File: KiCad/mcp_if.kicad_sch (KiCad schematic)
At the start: 11 parts

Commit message: Made the board :D
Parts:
- D10, D12, D8: footprint Diode_THT:D_5W_P5.08mm_Vertical_KathodeUp -> LED_THT:LED_D5.0mm
- D11, D13, D9: footprint Diode_THT:D_5W_P5.08mm_Vertical_AnodeUp -> LED_THT:LED_D5.0mm
- R10, R11, R9: footprint Resistor_THT:R_Axial_DIN0204_L3.6mm_D1.6mm_P2.54mm_Vertical -> Resistor_THT:R_Axial_DIN0207_L6.3mm_D2.5mm_P7.62mm_Horizontal
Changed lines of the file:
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@@
 			)
 		)
-		(property "Footprint" "Diode_THT:D_5W_P5.08mm_Vertical_AnodeUp"
+		(property "Footprint" "LED_THT:LED_D5.0mm"
 			(at 48.26 62.23 0)
 			(effects
@@
 			)
 		)
-		(property "Footprint" "Resistor_THT:R_Axial_DIN0204_L3.6mm_D1.6mm_P2.54mm_Vertical"
+		(property "Footprint" "Resistor_THT:R_Axial_DIN0207_L6.3mm_D2.5mm_P7.62mm_Horizontal"
 			(at 139.7 58.42 0)
 			(effects
@@
 			)
 		)
-		(property "Footprint" "Diode_THT:D_5W_P5.08mm_Vertical_KathodeUp"
+		(property "Footprint" "LED_THT:LED_D5.0mm"
 			(at 148.59 33.02 0)
 			(effects
@@
 			)
 		)
-		(property "Footprint" "Diode_THT:D_5W_P5.08mm_Vertical_AnodeUp"
+		(property "Footprint" "LED_THT:LED_D5.0mm"
 			(at 148.59 40.64 0)
 			(effects
@@
 			)
 		)
-		(property "Footprint" "Diode_THT:D_5W_P5.08mm_Vertical_KathodeUp"
+		(property "Footprint" "LED_THT:LED_D5.0mm"
 			(at 148.59 54.61 0)
 			(effects
@@
 			)
 		)
-		(property "Footprint" "Diode_THT:D_5W_P5.08mm_Vertical_AnodeUp"
+		(property "Footprint" "LED_THT:LED_D5.0mm"
 			(at 148.59 62.23 0)
 			(effects
@@
 			)
 		)
-		(property "Footprint" "Diode_THT:D_5W_P5.08mm_Vertical_KathodeUp"
+		(property "Footprint" "LED_THT:LED_D5.0mm"
 			(at 48.26 54.61 0)
 			(effects
@@
 			)
 		)
-		(property "Footprint" "Resistor_THT:R_Axial_DIN0204_L3.6mm_D1.6mm_P2.54mm_Vertical"
+		(property "Footprint" "Resistor_THT:R_Axial_DIN0207_L6.3mm_D2.5mm_P7.62mm_Horizontal"
 			(at 39.37 58.42 0)
 			(effects
@@
 			)
 		)
-		(property "Footprint" "Resistor_THT:R_Axial_DIN0204_L3.6mm_D1.6mm_P2.54mm_Vertical"
+		(property "Footprint" "Resistor_THT:R_Axial_DIN0207_L6.3mm_D2.5mm_P7.62mm_Horizontal"
 			(at 139.7 36.83 0)
 			(effects

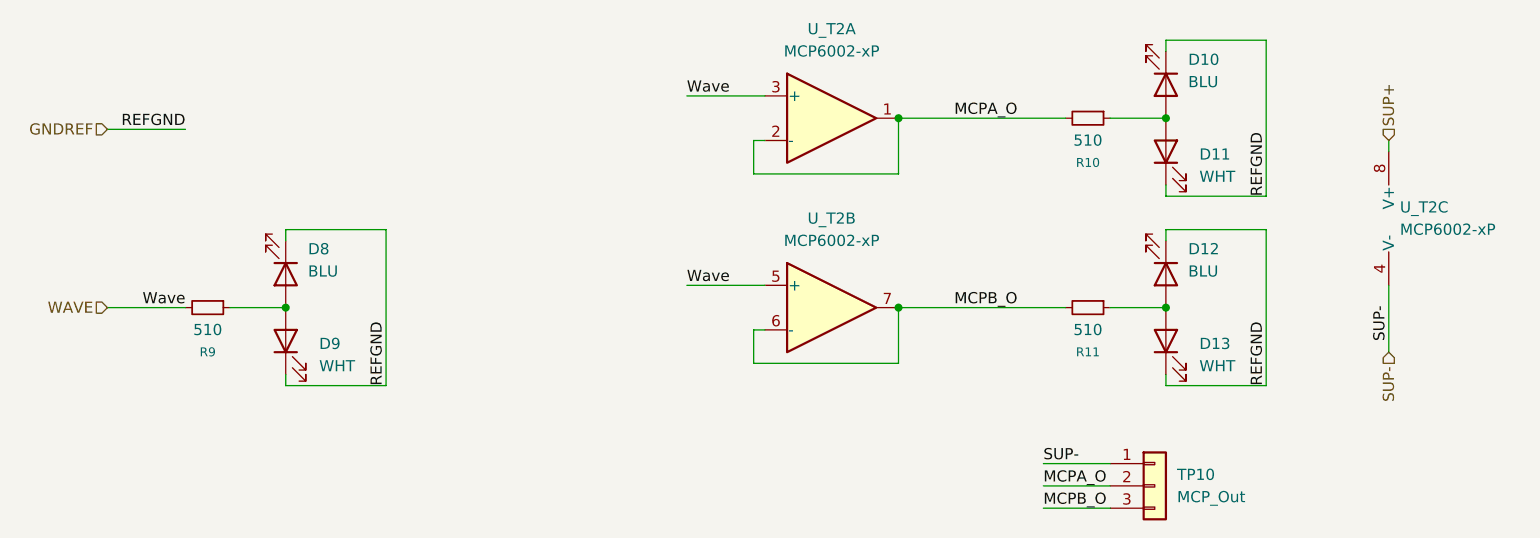
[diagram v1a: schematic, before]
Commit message: Added milling machine files / updated schematic+pcb annotations /  updated footprints
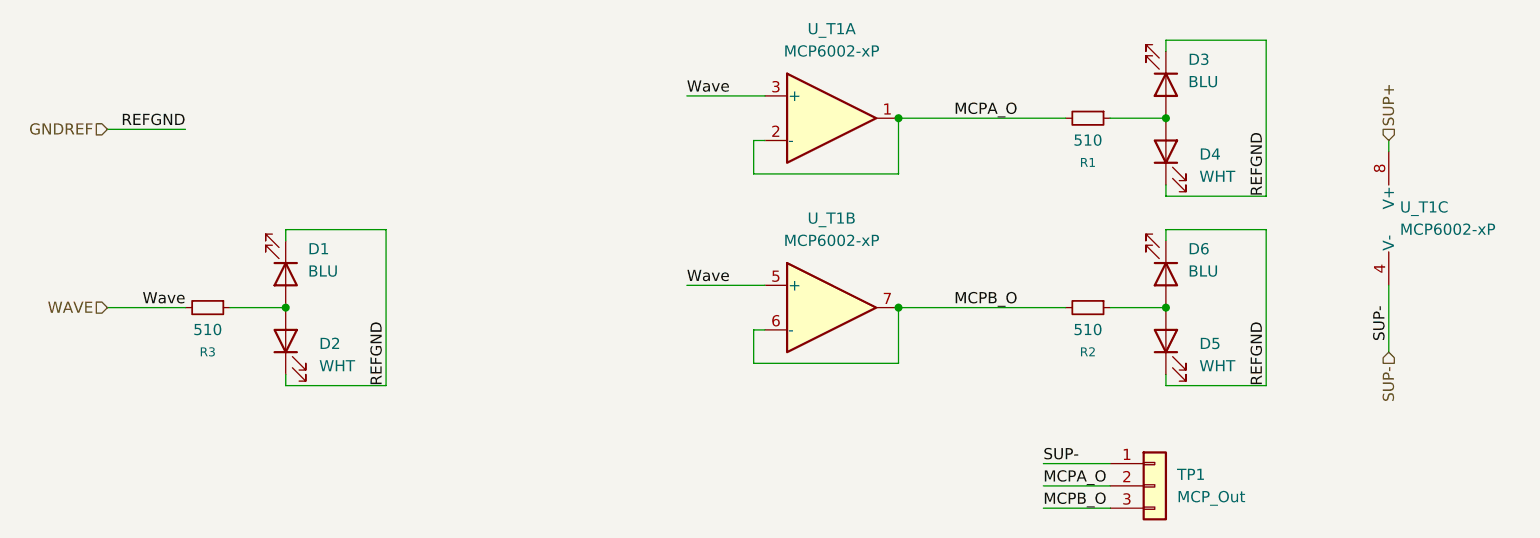
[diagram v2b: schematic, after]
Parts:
- renumbered D8 to D1, D9 to D2, D10 to D3, D11 to D4, D13 to D5, D12 to D6, R10 to R1, R11 to R2, R9 to R3, TP10 to TP1, U_T2 to U_T1
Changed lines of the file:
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@@
 		(dnp no)
 		(fields_autoplaced yes)
-		(property "Reference" "D9"
+		(property "Reference" "D2"
 			(at 52.07 62.5474 90)
 			(effects
@@
 			(project "ChipTester_354"
 				(path "/57b9e980-cd8f-44e4-af61-2cbd5bb30325/66abbfc5-c7ee-42ee-8f01-bf5211a4ea1c"
-					(reference "D9")
+					(reference "D2")
 					(unit 1)
 				)
@@
 		(dnp no)
 		(fields_autoplaced yes)
-		(property "Reference" "U_T2"
+		(property "Reference" "U_T1"
 			(at 175.26 46.9899 0)
 			(effects
@@
 			(project ""
 				(path "/57b9e980-cd8f-44e4-af61-2cbd5bb30325/66abbfc5-c7ee-42ee-8f01-bf5211a4ea1c"
-					(reference "U_T2")
+					(reference "U_T1")
 					(unit 3)
 				)
@@
 		(on_board yes)
 		(dnp no)
-		(property "Reference" "R11"
+		(property "Reference" "R2"
 			(at 139.7 63.5 90)
 			(effects
@@
 			(project "ChipTester_354"
 				(path "/57b9e980-cd8f-44e4-af61-2cbd5bb30325/66abbfc5-c7ee-42ee-8f01-bf5211a4ea1c"
-					(reference "R11")
+					(reference "R2")
 					(unit 1)
 				)
@@
 		(dnp no)
 		(fields_autoplaced yes)
-		(property "Reference" "D10"
+		(property "Reference" "D3"
 			(at 151.13 30.1624 90)
 			(effects
@@
 			(project "ChipTester_354"
 				(path "/57b9e980-cd8f-44e4-af61-2cbd5bb30325/66abbfc5-c7ee-42ee-8f01-bf5211a4ea1c"
-					(reference "D10")
+					(reference "D3")
 					(unit 1)
 				)
@@
 		(dnp no)
 		(fields_autoplaced yes)
-		(property "Reference" "U_T2"
+		(property "Reference" "U_T1"
 			(at 110.49 48.26 0)
 			(effects
@@
 			(project ""
 				(path "/57b9e980-cd8f-44e4-af61-2cbd5bb30325/66abbfc5-c7ee-42ee-8f01-bf5211a4ea1c"
-					(reference "U_T2")
+					(reference "U_T1")
 					(unit 2)
 				)
@@
 		(dnp no)
 		(fields_autoplaced yes)
-		(property "Reference" "D11"
+		(property "Reference" "D4"
 			(at 152.4 40.9574 90)
 			(effects
@@
 			(project "ChipTester_354"
 				(path "/57b9e980-cd8f-44e4-af61-2cbd5bb30325/66abbfc5-c7ee-42ee-8f01-bf5211a4ea1c"
-					(reference "D11")
+					(reference "D4")
 					(unit 1)
 				)
@@
 		(dnp no)
 		(fields_autoplaced yes)
-		(property "Reference" "D12"
+		(property "Reference" "D6"
 			(at 151.13 51.7524 90)
 			(effects
@@
 			(project "ChipTester_354"
 				(path "/57b9e980-cd8f-44e4-af61-2cbd5bb30325/66abbfc5-c7ee-42ee-8f01-bf5211a4ea1c"
-					(reference "D12")
+					(reference "D6")
 					(unit 1)
 				)
@@
 		(dnp no)
 		(fields_autoplaced yes)
-		(property "Reference" "D13"
+		(property "Reference" "D5"
 			(at 152.4 62.5474 90)
 			(effects
@@
 			(project "ChipTester_354"
 				(path "/57b9e980-cd8f-44e4-af61-2cbd5bb30325/66abbfc5-c7ee-42ee-8f01-bf5211a4ea1c"
-					(reference "D13")
+					(reference "D5")
 					(unit 1)
 				)
@@
 		(dnp no)
 		(fields_autoplaced yes)
-		(property "Reference" "U_T2"
+		(property "Reference" "U_T1"
 			(at 110.49 26.67 0)
 			(effects
@@
 			(project ""
 				(path "/57b9e980-cd8f-44e4-af61-2cbd5bb30325/66abbfc5-c7ee-42ee-8f01-bf5211a4ea1c"
-					(reference "U_T2")
+					(reference "U_T1")
 					(unit 1)
 				)
@@
 		(dnp no)
 		(fields_autoplaced yes)
-		(property "Reference" "D8"
+		(property "Reference" "D1"
 			(at 50.8 51.7524 90)
 			(effects
@@
 			(project "ChipTester_354"
 				(path "/57b9e980-cd8f-44e4-af61-2cbd5bb30325/66abbfc5-c7ee-42ee-8f01-bf5211a4ea1c"
-					(reference "D8")
+					(reference "D1")
 					(unit 1)
 				)
@@
 		(dnp no)
 		(fields_autoplaced yes)
-		(property "Reference" "TP10"
+		(property "Reference" "TP1"
 			(at 149.86 77.4699 0)
 			(effects
@@
 			(project ""
 				(path "/57b9e980-cd8f-44e4-af61-2cbd5bb30325/66abbfc5-c7ee-42ee-8f01-bf5211a4ea1c"
-					(reference "TP10")
+					(reference "TP1")
 					(unit 1)
 				)
@@
 		(on_board yes)
 		(dnp no)
-		(property "Reference" "R9"
+		(property "Reference" "R3"
 			(at 39.37 63.5 90)
 			(effects
@@
 			(project "ChipTester_354"
 				(path "/57b9e980-cd8f-44e4-af61-2cbd5bb30325/66abbfc5-c7ee-42ee-8f01-bf5211a4ea1c"
-					(reference "R9")
+					(reference "R3")
 					(unit 1)
 				)
@@
 		(on_board yes)
 		(dnp no)
-		(property "Reference" "R10"
+		(property "Reference" "R1"
 			(at 139.7 41.91 90)
 			(effects
@@
 			(project "ChipTester_354"
 				(path "/57b9e980-cd8f-44e4-af61-2cbd5bb30325/66abbfc5-c7ee-42ee-8f01-bf5211a4ea1c"
-					(reference "R10")
-					(unit 1)
-				)
+					(reference "R1")
+					(unit 1)
+				)
